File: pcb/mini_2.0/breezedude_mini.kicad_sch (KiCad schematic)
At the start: 43 parts, among them J1 USB_C_Receptacle_USB2.0_16P, J2 Conn_01x02_Socket, J3 Conn_01x04_Pin, J4 Conn_01x02_Pin, J5 Conn_01x04_Pin, J6 Conn_01x04_Pin, J7 Conn_01x02_Pin, Q1 PMOS, SW1 SW_Push, U1 ATSAMD21G18A-A, U2 RFM95W-868S2, U3 BMP280, U4 AP2112K-3.3, U5 PMIC-CN3063_SOIC8_, U6 BMP388

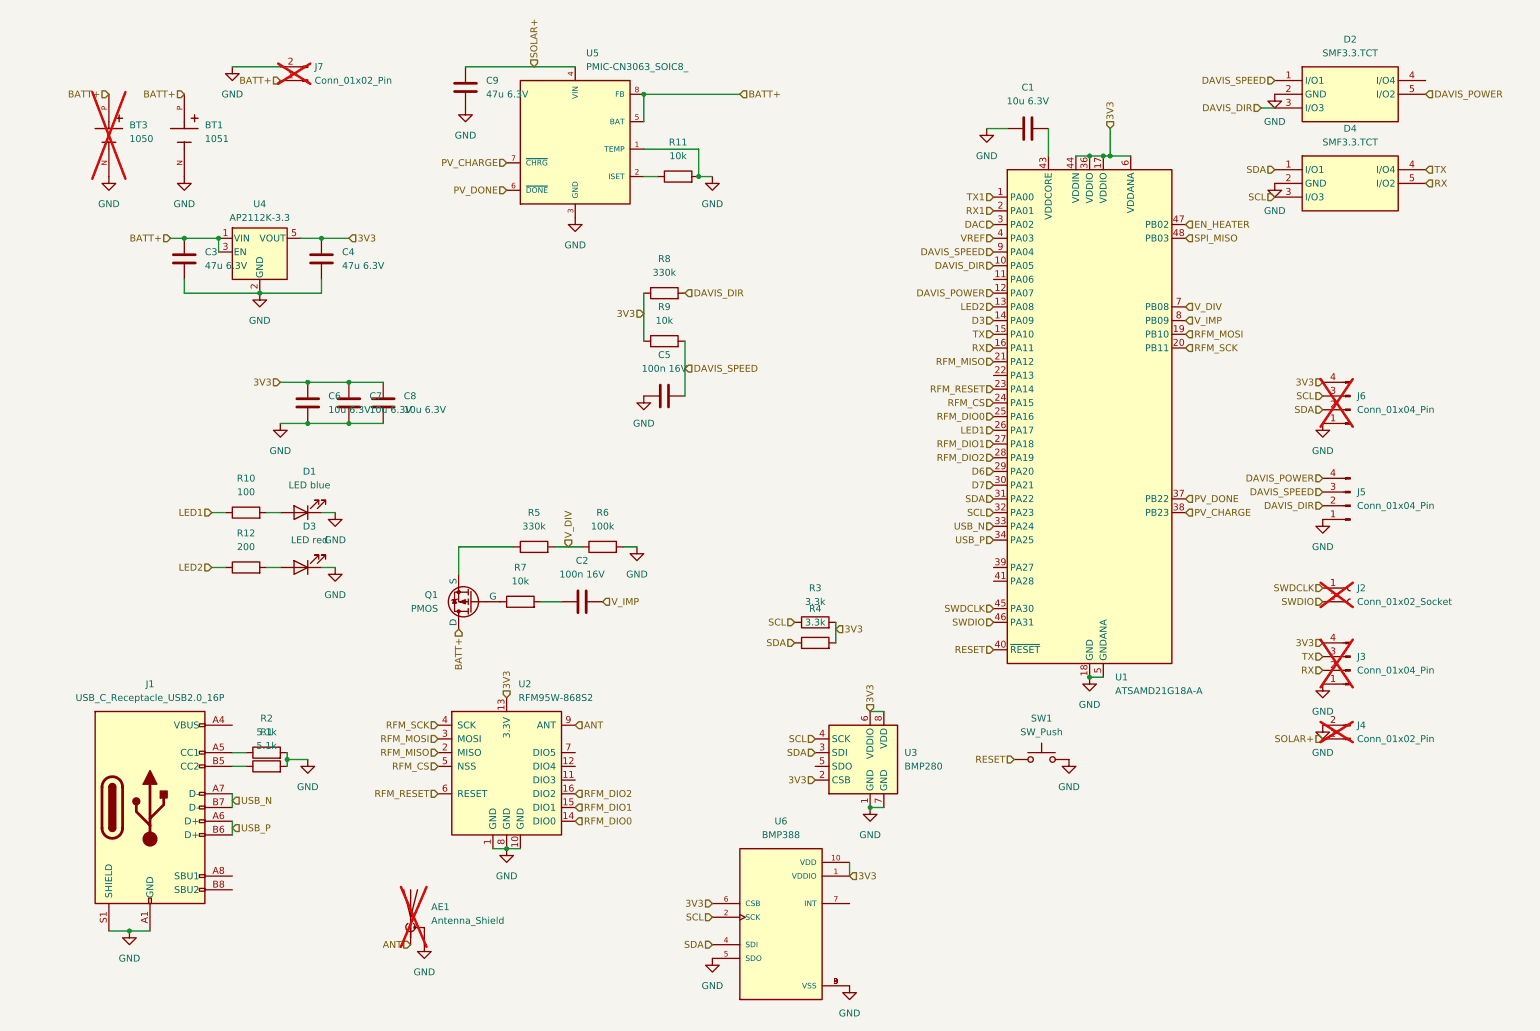
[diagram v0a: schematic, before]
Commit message: v2.1. fixed p-fet, added vollgo cc68, vertical SMA
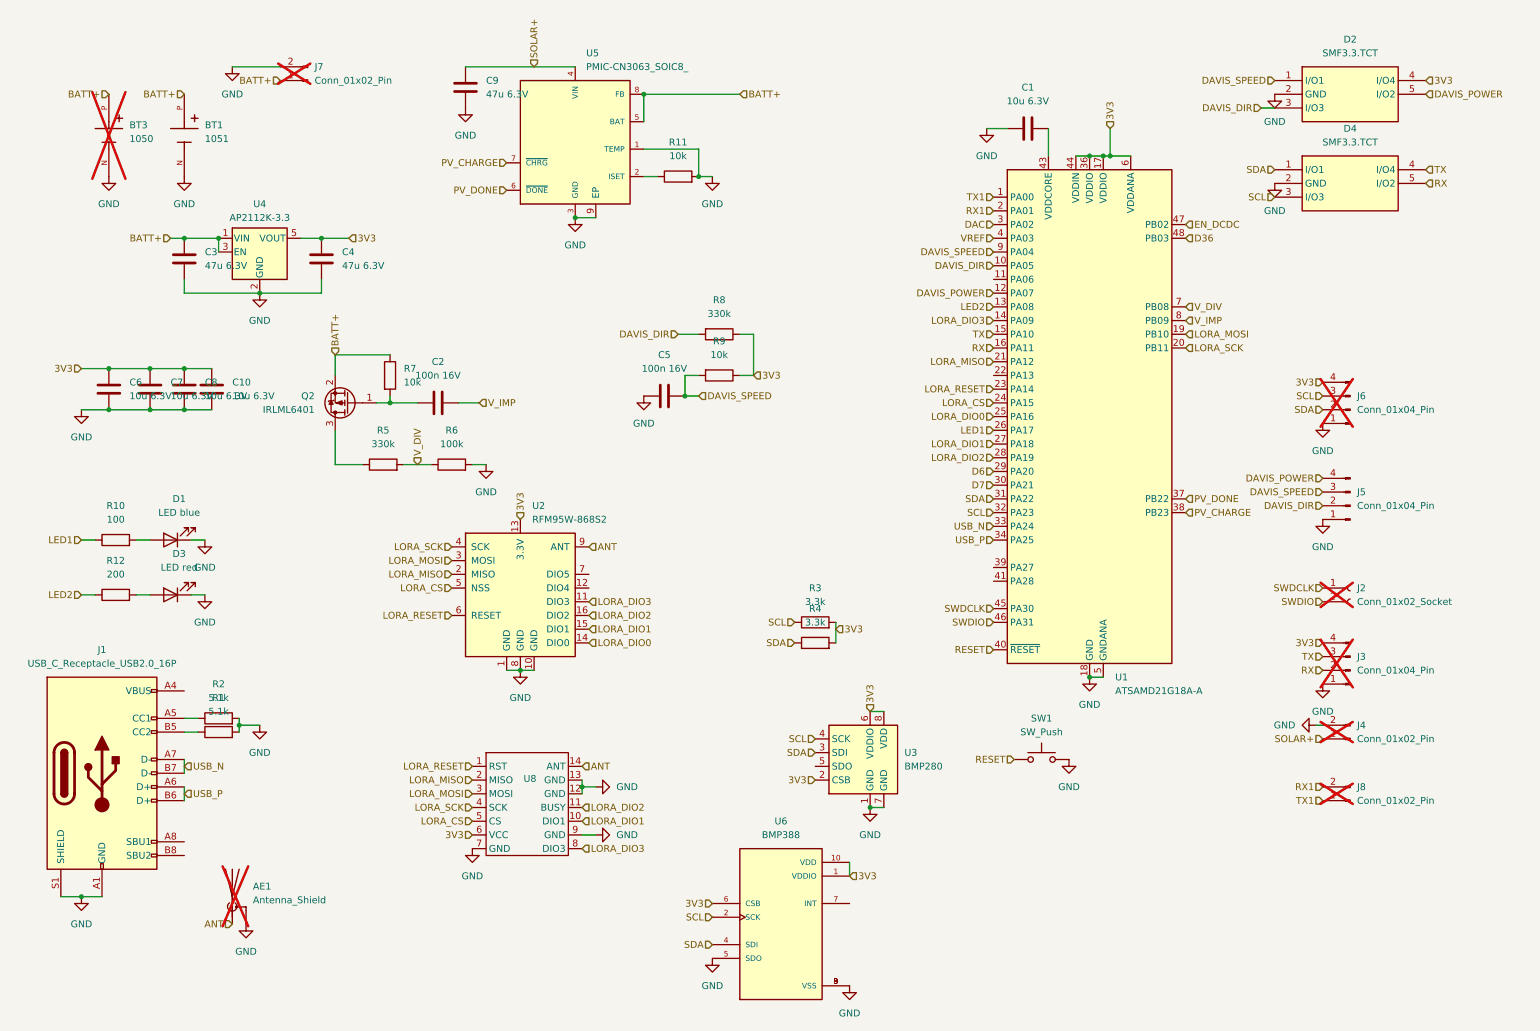
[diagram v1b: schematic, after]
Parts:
- removed Q1: PMOS, Package_TO_SOT_SMD:SOT-23-3, symbol Simulation_SPICE:PMOS
- added C10: 10u 6.3V, Capacitor_SMD:C_0402_1005Metric, symbol Device:C
- added J8: Conn_01x02_Pin, general:SolderJumper-2_Open_Gap1mm, symbol Connector:Conn_01x02_Pin
- added Q2: IRLML6401, Package_TO_SOT_SMD:SOT-23, symbol Transistor_FET:IRLML6401
- added U8: ~, LoRa:vollgo_vgdd79s868n0s1, symbol LoRa:vollgo_vgdd79s868n0s1
- AE1: footprint Connector_Coaxial:SMA_Samtec_SMA-J-P-X-ST-EM1_EdgeMount -> LoRa:sma_edge_6.5mm_vert
- U5: footprint Package_SO:SOIC-8_3.9x4.9mm_P1.27mm -> Package_SO:Infineon_PG-DSO-8-43
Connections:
- net D3 is gone; now on net LORA_DIO3: U1.14 (PA09)
- net 3V3: now also D2.4 (I/O4), C10.2, U8.6 (VCC)
- net ANT: now also U8.14 (ANT)
- net BATT+: now also R7.1, Q2.2 (S)
- net GND: now also U5.9 (EP), C10.1, U8.12 (GND), U8.13 (GND), U8.7 (GND), U8.9 (GND)
- net RX1: now also J8.2 (Pin_2)
- net TX1: now also J8.1 (Pin_1)
- net at R5.1: now also Q2.3 (D)
- net at C2.1, R7.2: now also Q2.1 (G)
- net LORA_DIO3: now reaches U2.11 (DIO3)
- net LORA_DIO3: now also U8.8 (DIO3)
- net EN_HEATER renamed EN_DCDC
- net RFM_CS renamed LORA_CS
- net LORA_CS: now also U8.5 (CS)
- net RFM_DIO0 renamed LORA_DIO0
- net RFM_DIO1 renamed LORA_DIO1
- net LORA_DIO1: now also U8.10 (DIO1)
- net RFM_DIO2 renamed LORA_DIO2
- net LORA_DIO2: now also U8.11 (BUSY)
- net RFM_MISO renamed LORA_MISO
- net LORA_MISO: now also U8.2 (MISO)
- net RFM_MOSI renamed LORA_MOSI
- net LORA_MOSI: now also U8.3 (MOSI)
- net RFM_RESET renamed LORA_RESET
- net LORA_RESET: now also U8.1 (RST)
- net RFM_SCK renamed LORA_SCK
- net LORA_SCK: now also U8.4 (SCK)
- net SPI_MISO renamed D36
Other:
- moved on the sheet: AE1, C2, C6, C7, C8, D1, D3, J1, R1, R10, R12, R2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

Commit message: mini V2.2
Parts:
- removed BT1: 1051, footprints_flo:BAT_1051, symbol 1051:1051
- removed C7: 10u 6.3V, Capacitor_SMD:C_0402_1005Metric, symbol Device:C
- removed J2: Conn_01x02_Socket, Connector_PinHeader_1.00mm:PinHeader_1x02_P1.00mm_Vertical, symbol Connector:Conn_01x02_Socket
- removed R8: 330k, Resistor_SMD:R_0402_1005Metric, symbol Device:R
- removed U2: RFM95W-868S2, RF_Module:HOPERF_RFM9XW_SMD, symbol RF_Module:RFM95W-868S2
- added C11: 100n 16V, Capacitor_SMD:C_0402_1005Metric, symbol Device:C
- added C12: 47u 6.3V, Capacitor_SMD:C_0805_2012Metric, symbol Device:C
- added D5: Diode, Diode_SMD:D_SOD-123, symbol Diode:MBR0520LT
- added J4: Conn_01x03_Pin, Connector_PinHeader_1.00mm:PinHeader_1x03_P1.00mm_Vertical, symbol Connector:Conn_01x03_Pin
- added JP1: SolderJumper_2_Open, Jumper:SolderJumper-2_P1.3mm_Open_RoundedPad1.0x1.5mm, symbol Jumper:SolderJumper_2_Open
- added Q1: P-MOS, Package_TO_SOT_SMD:SOT-23, symbol Transistor_FET:IRLML6401
- added U4: LIS2MDL, Package_LGA:LGA-12_2x2mm_P0.5mm, symbol Sensor_Magnetic:LIS2MDL
- added U8: HP203B, Sensors:HP203B-LGA8, symbol YAR_Sensors:HP203B
- C10: value 10u 6.3V -> 220n 16V; LCSC C15525 -> (none); now not fitted
- D3: renamed from D1; LCSC C72041 -> C2288
- J3: renamed from J5; now not fitted
- J7: renamed from J1; LCSC C5187468 -> C393939
- Q2: value IRLML6401 -> P-MOS; LCSC (none) -> C15127
- R2: renamed from R9; value 10k -> 100k; LCSC C25744 -> C25741
- R6: renamed from R10; value 100 -> 470; LCSC C25076 -> C25117
- SW1: LCSC C116501 -> C2905184
- U2: renamed from U4; value AP2112K-3.3 -> STLQ015M33R; LCSC C51118 -> C136154; LCSC_alt (none) -> C51118
- U5: renamed from U3; now not fitted
- U6: renamed from U8; LCSC (none) -> C2848400
- U7: renamed from U6; now not fitted
- renumbered BT3 to BT1, C9 to C1, C1 to C2, C2 to C9, D2 to D1, D4 to D2, D3 to D4, J7 to J1, J6 to J2, J3 to J5, J4 to J6, R11 to R1, R2 to R10, R1 to R11, R7 to R3, R5 to R4, R6 to R5, R12 to R7, R3 to R8, R4 to R9, U5 to U1, U1 to U3
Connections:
- net 3V3: now also C12.2, Q1.2 (S), U4.10 (Vdd_IO), U4.9 (Vdd), U8.3 (VDD), U8.8 (CSB); no longer C10.2, J5.4 (Pin_4)
- net GND: now also C10.2, C11.1, C12.1, J4.1 (Pin_1), U4.6 (GND), U4.8 (GND), U8.2 (GND); no longer C10.1
- net RESET: now also C11.2
- net SCL: now also U4.1 (SCL/SPC), U8.5 (SCL)
- net SDA: now also U4.4 (SDA/SDI/SDO), U8.6 (SDA)
- net SOLAR+: now also D5.1 (K)
- net SWDCLK: now also J4.3 (Pin_3)
- net SWDIO: now also J4.2 (Pin_2)
- net at J7.A4 (VBUS), J7.A9 (VBUS), J7.B4 (VBUS)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: now also JP1.1 (A)
- net D36 renamed SW_WS
- net SW_WS: now also Q1.1 (G)
- new net: D5.2 (A), JP1.2 (B)
- new net: C10.1, U4.5 (C1)
- new net VCC_WS: J5.4 (Pin_4), Q1.3 (D)
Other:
- moved on the sheet: C5, R2
